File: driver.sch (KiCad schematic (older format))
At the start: 52 parts, among them U10 LM5008MM, U11 SN74LVC1G66DBVR, U12 LM5107, U13 SN74LVC1G66DBVR, U14 TPS5430DDA, U15 LM5107, U2 SN74LVC1G66DBVR, U3 LM5107

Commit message: bug fixing
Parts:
- added U18: AQY282S, Package_SO:SO-4_4.4x4.3mm_P2.54mm, symbol Isolator:SFH617A-1
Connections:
- net EXT_OFF: now also U18.1; no longer R12.1, U10.6 (RON/SD)
- net GND: now also U18.2, U18.3
- new net EXT_OFF_DIRECT: R12.1, U10.6 (RON/SD), U18.4
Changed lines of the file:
@@
 Wire Wire Line
 	2300 5300 2250 5300
-Text HLabel 2000 5950 0    50   Input ~ 0
+Text HLabel 1250 6300 0    50   Input ~ 0
 EXT_OFF
 $Comp
@@
 Wire Wire Line
 	6600 5150 7300 5150
+$Comp
+L Isolator:SFH617A-1 U18
+U 1 1 5ED1E2BD
+P 1700 6400
+F 0 "U18" H 1700 6725 50  0000 C CNN
+F 1 "AQY282S" H 1700 6634 50  0000 C CNN
+F 2 "Package_SO:SO-4_4.4x4.3mm_P2.54mm" H 1500 6200 50  0001 L CIN
+F 3 "http://www.vishay.com/docs/83740/sfh617a.pdf" H 1700 6400 50  0001 L CNN
+	1    1700 6400
+	1    0    0    -1
+$EndComp
+Wire Wire Line
+	1250 6300 1400 6300
+Wire Wire Line
+	2000 5950 2000 6300
+$Comp
+L power:GND #PWR0163
+U 1 1 5ED390D4
+P 2000 6500
+F 0 "#PWR0163" H 2000 6250 50  0001 C CNN
+F 1 "GND" H 2005 6327 50  0000 C CNN
+F 2 "" H 2000 6500 50  0001 C CNN
+F 3 "" H 2000 6500 50  0001 C CNN
+	1    2000 6500
+	1    0    0    -1
+$EndComp
+$Comp
+L power:GND #PWR0164
+U 1 1 5ED39149
+P 1400 6500
+F 0 "#PWR0164" H 1400 6250 50  0001 C CNN
+F 1 "GND" H 1405 6327 50  0000 C CNN
+F 2 "" H 1400 6500 50  0001 C CNN
+F 3 "" H 1400 6500 50  0001 C CNN
+	1    1400 6500
+	1    0    0    -1
+$EndComp
+Text HLabel 1250 6050 0    50   Input ~ 0
+EXT_OFF_DIRECT
+Wire Wire Line
+	1250 6050 1500 6050
+Wire Wire Line
+	1500 6050 1500 5950
+Wire Wire Line
+	1500 5950 2000 5950
+Connection ~ 2000 5950
 $EndSCHEMATC

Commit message: add PDF
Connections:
- net at U14.5 (EN): now also U18.4
- net EXT_OFF renamed EN_3V3
- net EXT_OFF_DIRECT renamed EN_12V
- net EN_12V: no longer U18.4
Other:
- moved on the sheet: U18
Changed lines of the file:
@@
 	1650 5750 1650 5550
-Wire Wire Line
-	2550 5300 2300 5300
 Wire Wire Line
 	1950 5300 1900 5300
@@
 Wire Wire Line
 	1350 5750 1650 5750
-Wire Wire Line
-	2300 5300 2300 5950
-Wire Wire Line
-	2300 5950 2000 5950
-Connection ~ 2300 5300
-Wire Wire Line
-	2300 5300 2250 5300
-Text HLabel 1250 6300 0    50   Input ~ 0
-EXT_OFF
+Text HLabel 6500 6100 0    50   Input ~ 0
+EN_3V3
 $Comp
 L power:GND #PWR0146
@@
 Wire Wire Line
 	6600 5150 7300 5150
+Wire Wire Line
+	6500 6100 6650 6100
+Wire Wire Line
+	2250 5300 2300 5300
+Wire Wire Line
+	7300 5550 7250 5550
+Text HLabel 2200 6150 0    50   Input ~ 0
+EN_12V
+$Comp
+L power:GND #PWR0163
+U 1 1 5ED390D4
+P 7250 6300
+F 0 "#PWR0163" H 7250 6050 50  0001 C CNN
+F 1 "GND" H 7255 6127 50  0000 C CNN
+F 2 "" H 7250 6300 50  0001 C CNN
+F 3 "" H 7250 6300 50  0001 C CNN
+	1    7250 6300
+	1    0    0    -1
+$EndComp
+$Comp
+L power:GND #PWR0164
+U 1 1 5ED39149
+P 6650 6300
+F 0 "#PWR0164" H 6650 6050 50  0001 C CNN
+F 1 "GND" H 6655 6127 50  0000 C CNN
+F 2 "" H 6650 6300 50  0001 C CNN
+F 3 "" H 6650 6300 50  0001 C CNN
+	1    6650 6300
+	1    0    0    -1
+$EndComp
 $Comp
 L Isolator:SFH617A-1 U18
 U 1 1 5ED1E2BD
-P 1700 6400
-F 0 "U18" H 1700 6725 50  0000 C CNN
-F 1 "AQY282S" H 1700 6634 50  0000 C CNN
-F 2 "Package_SO:SO-4_4.4x4.3mm_P2.54mm" H 1500 6200 50  0001 L CIN
-F 3 "http://www.vishay.com/docs/83740/sfh617a.pdf" H 1700 6400 50  0001 L CNN
-	1    1700 6400
-	1    0    0    -1
-$EndComp
-Wire Wire Line
-	1250 6300 1400 6300
-Wire Wire Line
-	2000 5950 2000 6300
-$Comp
-L power:GND #PWR0163
-U 1 1 5ED390D4
-P 2000 6500
-F 0 "#PWR0163" H 2000 6250 50  0001 C CNN
-F 1 "GND" H 2005 6327 50  0000 C CNN
-F 2 "" H 2000 6500 50  0001 C CNN
-F 3 "" H 2000 6500 50  0001 C CNN
-	1    2000 6500
-	1    0    0    -1
-$EndComp
-$Comp
-L power:GND #PWR0164
-U 1 1 5ED39149
-P 1400 6500
-F 0 "#PWR0164" H 1400 6250 50  0001 C CNN
-F 1 "GND" H 1405 6327 50  0000 C CNN
-F 2 "" H 1400 6500 50  0001 C CNN
-F 3 "" H 1400 6500 50  0001 C CNN
-	1    1400 6500
-	1    0    0    -1
-$EndComp
-Text HLabel 1250 6050 0    50   Input ~ 0
-EXT_OFF_DIRECT
-Wire Wire Line
-	1250 6050 1500 6050
-Wire Wire Line
-	1500 6050 1500 5950
-Wire Wire Line
-	1500 5950 2000 5950
-Connection ~ 2000 5950
+P 6950 6200
+F 0 "U18" H 6950 6525 50  0000 C CNN
+F 1 "AQY282S" H 6950 6434 50  0000 C CNN
+F 2 "Package_SO:SO-4_4.4x4.3mm_P2.54mm" H 6750 6000 50  0001 L CIN
+F 3 "http://www.vishay.com/docs/83740/sfh617a.pdf" H 6950 6200 50  0001 L CNN
+	1    6950 6200
+	1    0    0    -1
+$EndComp
+Wire Wire Line
+	7250 5550 7250 6100
+Wire Wire Line
+	2300 5300 2300 6150
+Wire Wire Line
+	2300 6150 2200 6150
+Connection ~ 2300 5300
+Wire Wire Line
+	2300 5300 2550 5300
 $EndSCHEMATC

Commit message: save
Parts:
- removed C31: 10n0, Capacitor_SMD:C_0805_2012Metric, symbol Device:C
- removed C33, C34: 100u, Capacitor_Tantalum_SMD:CP_EIA-3528-21_Kemet-B, symbol Device:CP
- removed D5: SS210, Diode_SMD:D_SMA, symbol Diode:B360
- removed D6: B5819W, Diode_SMD:D_SOD-123, symbol Device:D_Schottky
- removed L2: 15u0, Inductor_SMD:L_7.3x7.3_H4.5, symbol Device:L
- removed R27: 13k0, Resistor_SMD:R_0805_2012Metric, symbol Device:R
- removed R34: 7k50, Resistor_SMD:R_0805_2012Metric, symbol Device:R
- removed U14: TPS5430DDA, Package_SO:TI_SO-PowerPAD-8_ThermalVias, symbol Regulator_Switching:TPS5430DDA
- removed U18: AQY282S, Package_SO:SO-4_4.4x4.3mm_P2.54mm, symbol Isolator:SFH617A-1
- added C? (x2): 100n, Capacitor_SMD:C_0805_2012Metric, symbol Device:C
- added C? (x2): 22u/25V, Capacitor_SMD:C_0805_2012Metric, symbol Device:C
- added D?: PMLL4153,115, symbol Device:D
- added D?: SS110, Diode_SMD:D_SMA, symbol Diode:B360
- added D?: PMLL4153, symbol Device:D
- added L?: 4u70, Inductor_SMD:L_12x12mm_H6mm, symbol Device:L
- added R?: 34k0, symbol Device:R
- added R?: 11k0, symbol Device:R
- added U?: LMR12010YMKE_NOPB, SOT95P280X110-6N, symbol gesc:LMR12010YMKE_NOPB
- C19: value 100n -> 1u00
- C20: value 10n0 -> 100n
- C23: value 10n0 -> 2n20
- C28: value 10u0/25V -> 22u/25V
- D10, D8, D9: symbol gsvesc:SMMBD914LT3G -> gesc:SMMBD914LT3G
- D4: value SS210 -> SS110
- L1: value 470u -> 330u
- R12: value 680k -> 220k
- R15: value 680k -> 100k
- R16: value 10k0 -> 11k0
- U11, U13, U2: footprint gsvesc:M74VHC1GT66DTT1G -> gesc:M74VHC1GT66DTT1G; symbol gsvesc:M74VHC1GT66DTT1G -> gesc:M74VHC1GT66DTT1G
- U12, U15, U3: symbol gsvesc:LM5107 -> gesc:LM5107
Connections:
- net +12V: now also D?.2 (A), U?.5 (VIN)
- net GND: now also C?.2, C?.2, C?.2, D?.2 (A), R?.1, U?.2 (GND); no longer C17.2
- net VCC: now also C?.1, C?.1, D?.2 (A), L?.1, R?.1
- net at C19.1, U10.7 (VCC): now also D?.1 (K)
- new net: C17.2, C?.1
- new net: C?.1, U?.1 (BOOST)
- new net: R?.2, R?.2, U?.3 (FB)
- new net: C?.2, D?.1 (K), D?.1 (K), L?.2, U?.6 (SW)
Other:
- moved on the sheet: C16, C28

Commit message: save
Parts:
- removed D10, D8, D9: SMMBD914LT3G, Package_TO_SOT_SMD:SOT-23, symbol gesc:SMMBD914LT3G
- added D6: SS110, Diode_SMD:D_SMA, symbol Device:D_Schottky
- added R27: 10k0, Resistor_SMD:R_0805_2012Metric, symbol Device:R
- added U14: AQY282S, symbol Isolator:SFH617A-1
- D5, D7: renamed from D?; footprint (none) -> Diode_SMD:D_MiniMELF
- R34, R44: renamed from R?; footprint (none) -> Resistor_SMD:R_0805_2012Metric
- U17: renamed from U?; footprint SOT95P280X110-6N -> gesc:SOT95P280X110-6N
- gave numbers to parts that had none: 6
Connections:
- net +12V: now also D6.1 (K), R27.1
- net EN_3V3: now also U14.1
- net GND: now also U14.2, U14.3
- net at U17.4 (EN): now also R27.2, U14.4
- new net VBUS: D6.2 (A)
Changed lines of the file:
@@
 Wire Wire Line
 	1150 1050 1150 1000
-Wire Wire Line
-	6500 1000 7000 1000
-$Comp
-L gesc:SMMBD914LT3G D8
-U 1 1 5EA7F038
-P 7450 750
-F 0 "D8" H 7450 534 50  0000 C CNN
-F 1 "SMMBD914LT3G" H 7450 625 50  0000 C CNN
-F 2 "Package_TO_SOT_SMD:SOT-23" H 7450 750 50  0001 C CNN
-F 3 "~" H 7450 750 50  0001 C CNN
-F 4 "C8598" H 7450 750 50  0001 C CNN "LCSC"
-	1    7450 750
-	-1   0    0    1
-$EndComp
-Wire Wire Line
-	7000 1000 7000 750
-Wire Wire Line
-	7000 750  7300 750
-Wire Wire Line
-	8250 750  8250 1000
-Wire Wire Line
-	7600 750  8250 750
-Wire Wire Line
-	1150 1000 1650 1000
-Connection ~ 7000 1000
-Wire Wire Line
-	7000 1000 7150 1000
-Connection ~ 8250 1000
-Wire Wire Line
-	3850 1000 4350 1000
-$Comp
-L gesc:SMMBD914LT3G D10
-U 1 1 5EABE0CB
-P 4800 750
-F 0 "D10" H 4800 534 50  0000 C CNN
-F 1 "SMMBD914LT3G" H 4800 625 50  0000 C CNN
-F 2 "Package_TO_SOT_SMD:SOT-23" H 4800 750 50  0001 C CNN
-F 3 "~" H 4800 750 50  0001 C CNN
-F 4 "C8598" H 4800 750 50  0001 C CNN "LCSC"
-	1    4800 750
-	-1   0    0    1
-$EndComp
-Wire Wire Line
-	4350 1000 4350 750
-Wire Wire Line
-	4350 750  4650 750
-Wire Wire Line
-	5600 750  5600 1000
-Wire Wire Line
-	4950 750  5600 750
-Connection ~ 4350 1000
-Wire Wire Line
-	4350 1000 4500 1000
-Connection ~ 5600 1000
-$Comp
-L gesc:SMMBD914LT3G D9
-U 1 1 5EACAF3E
-P 2100 750
-F 0 "D9" H 2100 534 50  0000 C CNN
-F 1 "SMMBD914LT3G" H 2100 625 50  0000 C CNN
-F 2 "Package_TO_SOT_SMD:SOT-23" H 2100 750 50  0001 C CNN
-F 3 "~" H 2100 750 50  0001 C CNN
-F 4 "C8598" H 2100 750 50  0001 C CNN "LCSC"
-	1    2100 750
-	-1   0    0    1
-$EndComp
-Wire Wire Line
-	1650 1000 1650 750
-Wire Wire Line
-	1650 750  1950 750
-Wire Wire Line
-	2900 750  2900 1000
-Wire Wire Line
-	2250 750  2900 750
-Connection ~ 1650 1000
-Wire Wire Line
-	1650 1000 1800 1000
-Connection ~ 2900 1000
 $Comp
 L power:GND #PWR0151
@@
 L power:GND #PWR0163
 U 1 1 5ED390D4
-P 7250 6300
-F 0 "#PWR0163" H 7250 6050 50  0001 C CNN
-F 1 "GND" H 7255 6127 50  0000 C CNN
-F 2 "" H 7250 6300 50  0001 C CNN
-F 3 "" H 7250 6300 50  0001 C CNN
-	1    7250 6300
+P 6800 6250
+F 0 "#PWR0163" H 6800 6000 50  0001 C CNN
+F 1 "GND" H 6805 6077 50  0000 C CNN
+F 2 "" H 6800 6250 50  0001 C CNN
+F 3 "" H 6800 6250 50  0001 C CNN
+	1    6800 6250
 	1    0    0    -1
 $EndComp
@@
 L power:GND #PWR0164
 U 1 1 5ED39149
-P 6650 6300
-F 0 "#PWR0164" H 6650 6050 50  0001 C CNN
-F 1 "GND" H 6655 6127 50  0000 C CNN
-F 2 "" H 6650 6300 50  0001 C CNN
-F 3 "" H 6650 6300 50  0001 C CNN
-	1    6650 6300
+P 6200 6250
+F 0 "#PWR0164" H 6200 6000 50  0001 C CNN
+F 1 "GND" H 6205 6077 50  0000 C CNN
+F 2 "" H 6200 6250 50  0001 C CNN
+F 3 "" H 6200 6250 50  0001 C CNN
+	1    6200 6250
 	1    0    0    -1
 $EndComp
@@
 	2250 5300 2300 5300
 Wire Wire Line
-	6500 6100 6650 6100
+	6050 6050 6200 6050
 $Comp
 L Device:R R38
@@
 	1    0    0    -1
 $EndComp
-Text HLabel 6500 6100 0    50   Input ~ 0
+Text HLabel 6050 6050 0    50   Input ~ 0
 EN_3V3
 Wire Wire Line
@@
 $EndComp
 $Comp
-L gesc:LMR12010YMKE_NOPB U?
+L gesc:LMR12010YMKE_NOPB U17
 U 1 1 6013A5DC
 P 7800 5300
-F 0 "U?" H 7800 5870 50  0000 C CNN
+F 0 "U17" H 7800 5870 50  0000 C CNN
 F 1 "LMR12010YMKE_NOPB" H 7800 5779 50  0000 C CNN
-F 2 "SOT95P280X110-6N" H 7800 5300 50  0001 L BNN
+F 2 "gesc:SOT95P280X110-6N" H 7800 5300 50  0001 L BNN
 F 3 "" H 7800 5300 50  0001 L BNN
 	1    7800 5300
@@
 $EndComp
 $Comp
-L Device:C C?
+L Device:C C31
 U 1 1 6015CDD5
 P 1650 5800
-F 0 "C?" H 1765 5846 50  0000 L CNN
+F 0 "C31" H 1765 5846 50  0000 L CNN
 F 1 "100n" H 1765 5755 50  0000 L CNN
 F 2 "Capacitor_SMD:C_0805_2012Metric" H 1688 5650 50  0001 C CNN
@@
 	1050 5750 1050 6150
 $Comp
-L Device:D D?
+L Device:D D5
 U 1 1 601823EE
 P 3150 4750
-F 0 "D?" H 3150 4533 50  0000 C CNN
+F 0 "D5" H 3150 4533 50  0000 C CNN
 F 1 " PMLL4153,115 " H 3150 4624 50  0000 C CNN
-F 2 "" H 3150 4750 50  0001 C CNN
+F 2 "Diode_SMD:D_MiniMELF" H 3150 4750 50  0001 C CNN
 F 3 "~" H 3150 4750 50  0001 C CNN
 	1    3150 4750
@@
 	1    0    0    -1
 $EndComp
-Wire Wire Line
-	6450 5100 7100 5100
 Connection ~ 6450 5100
 $Comp
-L Diode:B360 D?
+L Diode:B360 D8
 U 1 1 601BB258
 P 8950 5350
-F 0 "D?" V 8904 5429 50  0000 L CNN
+F 0 "D8" V 8904 5429 50  0000 L CNN
 F 1 "SS110" V 8995 5429 50  0000 L CNN
 F 2 "Diode_SMD:D_SMA" H 8950 5175 50  0001 C CNN
@@
 Connection ~ 8950 5500
 $Comp
-L Device:L L?
+L Device:L L2
 U 1 1 601E07CC
 P 9500 5200
-F 0 "L?" V 9450 5200 50  0000 C CNN
+F 0 "L2" V 9450 5200 50  0000 C CNN
 F 1 "4u70" V 9600 5200 50  0000 C CNN
 F 2 "Inductor_SMD:L_12x12mm_H6mm" H 9500 5200 50  0001 C CNN
@@
 Connection ~ 8950 5200
 $Comp
-L Device:C C?
+L Device:C C34
 U 1 1 601ECA0B
 P 9750 5350
-F 0 "C?" H 9865 5396 50  0000 L CNN
+F 0 "C34" H 9865 5396 50  0000 L CNN
 F 1 "22u/25V" H 9865 5305 50  0000 L CNN
 F 2 "Capacitor_SMD:C_0805_2012Metric" H 9788 5200 50  0001 C CNN
@@
 $EndComp
 $Comp
-L Device:C C?
+L Device:C C50
 U 1 1 601ED2B2
 P 10350 5350
-F 0 "C?" H 10465 5396 50  0000 L CNN
+F 0 "C50" H 10465 5396 50  0000 L CNN
 F 1 "22u/25V" H 10465 5305 50  0000 L CNN
 F 2 "Capacitor_SMD:C_0805_2012Metric" H 10388 5200 50  0001 C CNN
@@
 Connection ~ 9750 5500
 $Comp
-L Device:C C?
+L Device:C C33
 U 1 1 6022B6B6
 P 8750 5000
-F 0 "C?" V 9002 5000 50  0000 C CNN
+F 0 "C33" V 9002 5000 50  0000 C CNN
 F 1 "100n" V 8911 5000 50  0000 C CNN
 F 2 "Capacitor_SMD:C_0805_2012Metric" H 8788 4850 50  0001 C CNN
@@
 	9400 5100 9750 5100
 $Comp
-L Device:R R?
+L Device:R R44
 U 1 1 60245263
 P 9250 5100
-F 0 "R?" V 9043 5100 50  0000 C CNN
+F 0 "R44" V 9043 5100 50  0000 C CNN
 F 1 "34k0" V 9134 5100 50  0000 C CNN
-F 2 "" V 9180 5100 50  0001 C CNN
+F 2 "Resistor_SMD:R_0805_2012Metric" V 9180 5100 50  0001 C CNN
 F 3 "~" H 9250 5100 50  0001 C CNN
 	1    9250 5100
@@
 $EndComp
 $Comp
-L Device:R R?
+L Device:R R34
 U 1 1 6026DD04
 P 9050 4750
-F 0 "R?" H 9120 4796 50  0000 L CNN
+F 0 "R34" H 9120 4796 50  0000 L CNN
 F 1 "11k0" H 9120 4705 50  0000 L CNN
-F 2 "" V 8980 4750 50  0001 C CNN
+F 2 "Resistor_SMD:R_0805_2012Metric" V 8980 4750 50  0001 C CNN
 F 3 "~" H 9050 4750 50  0001 C CNN
 	1    9050 4750
@@
 	9050 4600 9050 4550
 $Comp
-L power:GND #PWR?
+L power:GND #PWR0160
 U 1 1 60287A4C
 P 9050 4550
-F 0 "#PWR?" H 9050 4300 50  0001 C CNN
+F 0 "#PWR0160" H 9050 4300 50  0001 C CNN
 F 1 "GND" H 9055 4377 50  0000 C CNN
 F 2 "" H 9050 4550 50  0001 C CNN
@@
 $EndComp
 $Comp
-L Device:D D?
+L Device:D D7
 U 1 1 602885F0
 P 8450 4600
-F 0 "D?" H 8450 4383 50  0000 C CNN
+F 0 "D7" H 8450 4383 50  0000 C CNN
 F 1 "PMLL4153" H 8450 4474 50  0000 C CNN
-F 2 "" H 8450 4600 50  0001 C CNN
+F 2 "Diode_SMD:D_MiniMELF" H 8450 4600 50  0001 C CNN
 F 3 "~" H 8450 4600 50  0001 C CNN
 	1    8450 4600
@@
 	8050 4600 8050 4550
 $Comp
-L power:VCC #PWR?
+L power:VCC #PWR0161
 U 1 1 602A61C9
 P 8050 4550
-F 0 "#PWR?" H 8050 4400 50  0001 C CNN
+F 0 "#PWR0161" H 8050 4400 50  0001 C CNN
 F 1 "VCC" H 8067 4723 50  0000 C CNN
 F 2 "" H 8050 4550 50  0001 C CNN
@@
 	1    0    0    -1
 $EndComp
+$Comp
+L Isolator:SFH617A-1 U14
+U 1 1 600DB921
+P 6500 6150
+F 0 "U14" H 6500 6475 50  0000 C CNN
+F 1 "AQY282S" H 6500 6384 50  0000 C CNN
+F 2 "" H 6300 5950 50  0001 L CIN
+F 3 "http://www.vishay.com/docs/83740/sfh617a.pdf" H 6500 6150 50  0001 L CNN
+	1    6500 6150
+	1    0    0    -1
+$EndComp
+Wire Wire Line
+	7100 5000 7000 5000
+Wire Wire Line
+	7000 5000 7000 6050
+Wire Wire Line
+	7000 6050 6800 6050
+$Comp
+L Device:R R27
+U 1 1 600FD758
+P 7000 4750
+F 0 "R27" H 7070 4796 50  0000 L CNN
+F 1 "10k0" H 7070 4705 50  0000 L CNN
+F 2 "Resistor_SMD:R_0805_2012Metric" V 6930 4750 50  0001 C CNN
+F 3 "~" H 7000 4750 50  0001 C CNN
+	1    7000 4750
+	1    0    0    -1
+$EndComp
+Wire Wire Line
+	7000 4900 7000 5000
+Connection ~ 7000 5000
+$Comp
+L power:+12V #PWR0166
+U 1 1 6010B63A
+P 7000 4500
+F 0 "#PWR0166" H 7000 4350 50  0001 C CNN
+F 1 "+12V" H 7015 4673 50  0000 C CNN
+F 2 "" H 7000 4500 50  0001 C CNN
+F 3 "" H 7000 4500 50  0001 C CNN
+	1    7000 4500
+	1    0    0    -1
+$EndComp
+Wire Wire Line
+	7000 4500 7000 4600
+Wire Wire Line
+	1150 1000 1800 1000
+Wire Wire Line
+	3850 1000 4500 1000
+Wire Wire Line
+	6500 1000 7150 1000
+$Comp
+L Device:D_Schottky D6
+U 1 1 60167C08
+P 6300 4700
+F 0 "D6" H 6300 4483 50  0000 C CNN
+F 1 "SS110" H 6300 4574 50  0000 C CNN
+F 2 "Diode_SMD:D_SMA" H 6300 4700 50  0001 C CNN
+F 3 "~" H 6300 4700 50  0001 C CNN
+	1    6300 4700
+	-1   0    0    1
+$EndComp
+Wire Wire Line
+	6450 5100 7100 5100
+Wire Wire Line
+	6450 5100 6450 4700
+$Comp
+L power:VBUS #PWR0167
+U 1 1 60181AD6
+P 6000 4700
+F 0 "#PWR0167" H 6000 4550 50  0001 C CNN
+F 1 "VBUS" V 6015 4827 50  0000 L CNN
+F 2 "" H 6000 4700 50  0001 C CNN
+F 3 "" H 6000 4700 50  0001 C CNN
+	1    6000 4700
+	0    -1   -1   0
+$EndComp
+Wire Wire Line
+	6000 4700 6150 4700
 $EndSCHEMATC

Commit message: save
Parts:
- L1: footprint Inductor_SMD:L_12x12mm_H6mm -> Inductor_SMD:L_12x12mm_H4.5mm
- L2: footprint Inductor_SMD:L_12x12mm_H6mm -> Inductor_SMD:L_Wuerth_WE-PD2-Typ-L
- U14: footprint (none) -> Package_SO:SO-4_4.4x4.3mm_P2.54mm
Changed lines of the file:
@@
 F 0 "L1" V 4022 5300 50  0000 C CNN
 F 1 "330u" V 4113 5300 50  0000 C CNN
-F 2 "Inductor_SMD:L_12x12mm_H6mm" H 4200 5300 50  0001 C CNN
+F 2 "Inductor_SMD:L_12x12mm_H4.5mm" H 4200 5300 50  0001 C CNN
 F 3 "~" H 4200 5300 50  0001 C CNN
 F 4 "SWRB1207S-471MT" V 4200 5300 50  0001 C CNN "Partnumber"
@@
 F 0 "L2" V 9450 5200 50  0000 C CNN
 F 1 "4u70" V 9600 5200 50  0000 C CNN
-F 2 "Inductor_SMD:L_12x12mm_H6mm" H 9500 5200 50  0001 C CNN
+F 2 "Inductor_SMD:L_Wuerth_WE-PD2-Typ-L" H 9500 5200 50  0001 C CNN
 F 3 "~" H 9500 5200 50  0001 C CNN
 F 4 "SWRB1207S-471MT" V 9500 5200 50  0001 C CNN "Partnumber"
@@
 F 0 "U14" H 6500 6475 50  0000 C CNN
 F 1 "AQY282S" H 6500 6384 50  0000 C CNN
-F 2 "" H 6300 5950 50  0001 L CIN
+F 2 "Package_SO:SO-4_4.4x4.3mm_P2.54mm" H 6300 5950 50  0001 L CIN
 F 3 "http://www.vishay.com/docs/83740/sfh617a.pdf" H 6500 6150 50  0001 L CNN
 	1    6500 6150

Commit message: save
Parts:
- removed D5: PMLL4153,115, Diode_SMD:D_MiniMELF, symbol Device:D
- removed D7: PMLL4153, Diode_SMD:D_MiniMELF, symbol Device:D
- added D6: B5819W, Diode_SMD:D_SMA, symbol Device:D_Schottky
- added D7: B5819W, symbol Device:D_Schottky
- D5: renamed from D6; value SS110 -> B5819W
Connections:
- net +12V: now also D6.2 (A)
- net VCC: now also D7.2 (A)
- net at C19.1, U10.7 (VCC): now also D6.1 (K)
- net at C33.2, D8.1 (K), L2.2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: now also D7.1 (K)
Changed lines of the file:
@@
 	1050 5750 1050 6150
-$Comp
-L Device:D D5
-U 1 1 601823EE
-P 3150 4750
-F 0 "D5" H 3150 4533 50  0000 C CNN
-F 1 " PMLL4153,115 " H 3150 4624 50  0000 C CNN
-F 2 "Diode_SMD:D_MiniMELF" H 3150 4750 50  0001 C CNN
-F 3 "~" H 3150 4750 50  0001 C CNN
-	1    3150 4750
-	-1   0    0    1
-$EndComp
 $Comp
 L Device:C C28
@@
 	-1   0    0    1
 $EndComp
-$Comp
-L Device:D D7
-U 1 1 602885F0
-P 8450 4600
-F 0 "D7" H 8450 4383 50  0000 C CNN
-F 1 "PMLL4153" H 8450 4474 50  0000 C CNN
-F 2 "Diode_SMD:D_MiniMELF" H 8450 4600 50  0001 C CNN
-F 3 "~" H 8450 4600 50  0001 C CNN
-	1    8450 4600
-	-1   0    0    1
-$EndComp
 Wire Wire Line
 	8600 4600 8950 4600
@@
 	6500 1000 7150 1000
 $Comp
-L Device:D_Schottky D6
+L Device:D_Schottky D5
 U 1 1 60167C08
 P 6300 4700
-F 0 "D6" H 6300 4483 50  0000 C CNN
-F 1 "SS110" H 6300 4574 50  0000 C CNN
+F 0 "D5" H 6300 4483 50  0000 C CNN
+F 1 "B5819W" H 6300 4574 50  0000 C CNN
 F 2 "Diode_SMD:D_SMA" H 6300 4700 50  0001 C CNN
 F 3 "~" H 6300 4700 50  0001 C CNN
@@
 Wire Wire Line
 	6000 4700 6150 4700
+$Comp
+L Device:D_Schottky D7
+U 1 1 600EC395
+P 8450 4600
+F 0 "D7" H 8450 4383 50  0000 C CNN
+F 1 "B5819W" H 8450 4474 50  0000 C CNN
+F 2 "" H 8450 4600 50  0001 C CNN
+F 3 "~" H 8450 4600 50  0001 C CNN
+	1    8450 4600
+	-1   0    0    1
+$EndComp
+$Comp
+L Device:D_Schottky D6
+U 1 1 600EE496
+P 3150 4750
+F 0 "D6" H 3150 4533 50  0000 C CNN
+F 1 "B5819W" H 3150 4624 50  0000 C CNN
+F 2 "Diode_SMD:D_SMA" H 3150 4750 50  0001 C CNN
+F 3 "~" H 3150 4750 50  0001 C CNN
+	1    3150 4750
+	-1   0    0    1
+$EndComp
 $EndSCHEMATC

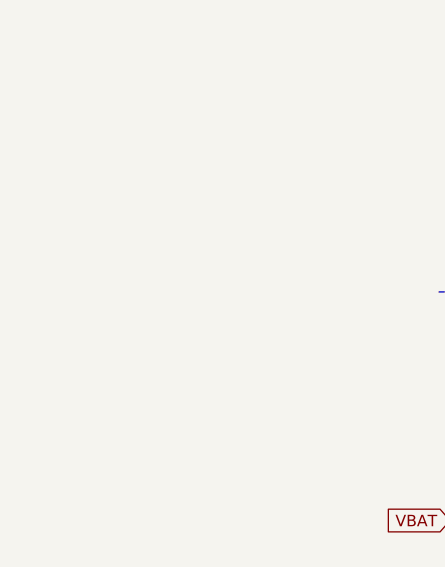
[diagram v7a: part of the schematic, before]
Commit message: PCB updated: - reroute SH_X - change 3V3 Power supply - add VBUS to 3V3 regulator - use LM5107 - change Layer/Plane assignment - move current sense tracks to layer 2
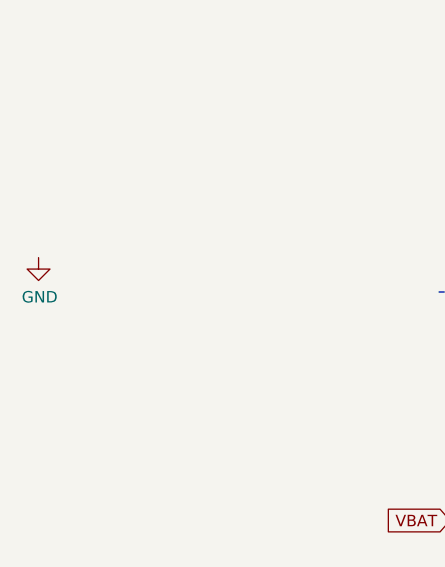
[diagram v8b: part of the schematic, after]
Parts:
- D5, D6: footprint Diode_SMD:D_SMA -> Diode_SMD:D_SOD-123
- D7: footprint (none) -> Diode_SMD:D_SOD-123
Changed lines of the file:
@@
 L power:GND #PWR0151
 U 1 1 5EB16BDB
-P 8950 5750
-F 0 "#PWR0151" H 8950 5500 50  0001 C CNN
-F 1 "GND" H 8955 5577 50  0000 C CNN
-F 2 "" H 8950 5750 50  0001 C CNN
-F 3 "" H 8950 5750 50  0001 C CNN
-	1    8950 5750
+P -850 4050
+F 0 "#PWR0151" H -850 3800 50  0001 C CNN
+F 1 "GND" H -845 3877 50  0000 C CNN
+F 2 "" H -850 4050 50  0001 C CNN
+F 3 "" H -850 4050 50  0001 C CNN
+	1    -850 4050
 	1    0    0    -1
 $EndComp
@@
 F 0 "D5" H 6300 4483 50  0000 C CNN
 F 1 "B5819W" H 6300 4574 50  0000 C CNN
-F 2 "Diode_SMD:D_SMA" H 6300 4700 50  0001 C CNN
+F 2 "Diode_SMD:D_SOD-123" H 6300 4700 50  0001 C CNN
 F 3 "~" H 6300 4700 50  0001 C CNN
 	1    6300 4700
@@
 F 0 "D7" H 8450 4383 50  0000 C CNN
 F 1 "B5819W" H 8450 4474 50  0000 C CNN
-F 2 "" H 8450 4600 50  0001 C CNN
+F 2 "Diode_SMD:D_SOD-123" H 8450 4600 50  0001 C CNN
 F 3 "~" H 8450 4600 50  0001 C CNN
 	1    8450 4600
@@
 F 0 "D6" H 3150 4533 50  0000 C CNN
 F 1 "B5819W" H 3150 4624 50  0000 C CNN
-F 2 "Diode_SMD:D_SMA" H 3150 4750 50  0001 C CNN
+F 2 "Diode_SMD:D_SOD-123" H 3150 4750 50  0001 C CNN
 F 3 "~" H 3150 4750 50  0001 C CNN
 	1    3150 4750
 	-1   0    0    1
 $EndComp
+$Comp
+L power:GND #PWR0168
+U 1 1 6010EE8C
+P 8950 5750
+F 0 "#PWR0168" H 8950 5500 50  0001 C CNN
+F 1 "GND" H 8955 5577 50  0000 C CNN
+F 2 "" H 8950 5750 50  0001 C CNN
+F 3 "" H 8950 5750 50  0001 C CNN
+	1    8950 5750
+	1    0    0    -1
+$EndComp
 $EndSCHEMATC
